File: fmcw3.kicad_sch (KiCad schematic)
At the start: 12 parts, among them P5 CONN_01X01, P7 CONN_01X01, P8 CONN_01X01, U4 ECS-TXO-3225MV, U6 NB3N551

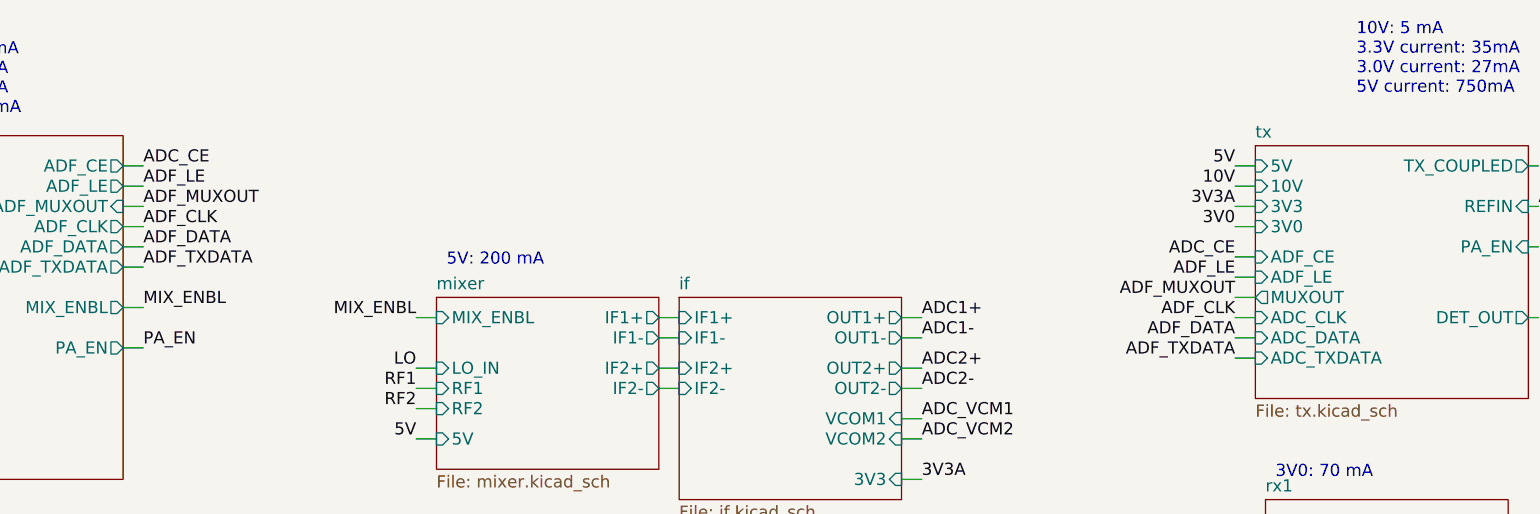
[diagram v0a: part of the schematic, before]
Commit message: 3 leds are added design is checked. Schematic pin name corrected
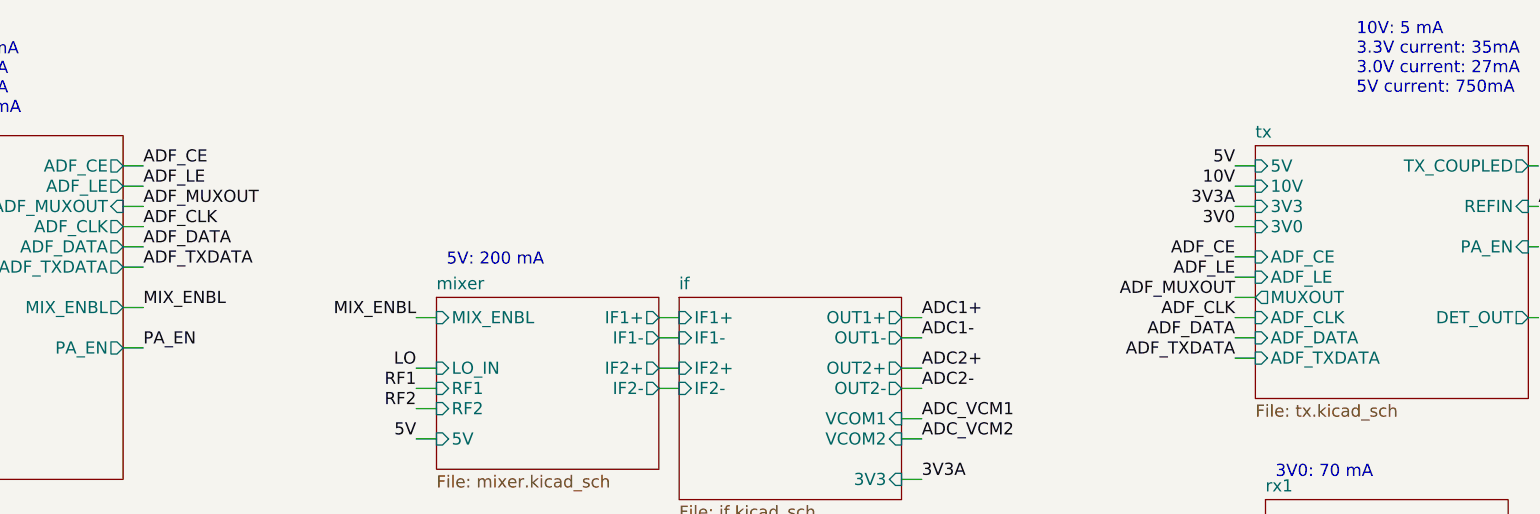
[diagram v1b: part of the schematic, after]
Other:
- sheet tx ports: added ADF_CLK, ADF_DATA, ADF_TXDATA; removed ADC_CLK, ADC_DATA, ADC_TXDATA
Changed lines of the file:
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@@
 		)
 	)
-	(label "ADC_CE"
+	(label "ADF_CE"
 		(at 83.82 46.99 0)
 		(effects
@@
 		)
 	)
-	(label "ADC_CE"
+	(label "ADF_CE"
 		(at 220.98 58.42 180)
 		(effects
@@
 			)
 		)
-		(pin "ADC_TXDATA" input
+		(pin "ADF_TXDATA" input
 			(at 223.52 71.12 180)
 			(effects
@@
 			)
 		)
-		(pin "ADC_CLK" input
+		(pin "ADF_CLK" input
 			(at 223.52 66.04 180)
 			(effects
@@
 			)
 		)
-		(pin "ADC_DATA" input
+		(pin "ADF_DATA" input
 			(at 223.52 68.58 180)
 			(effects

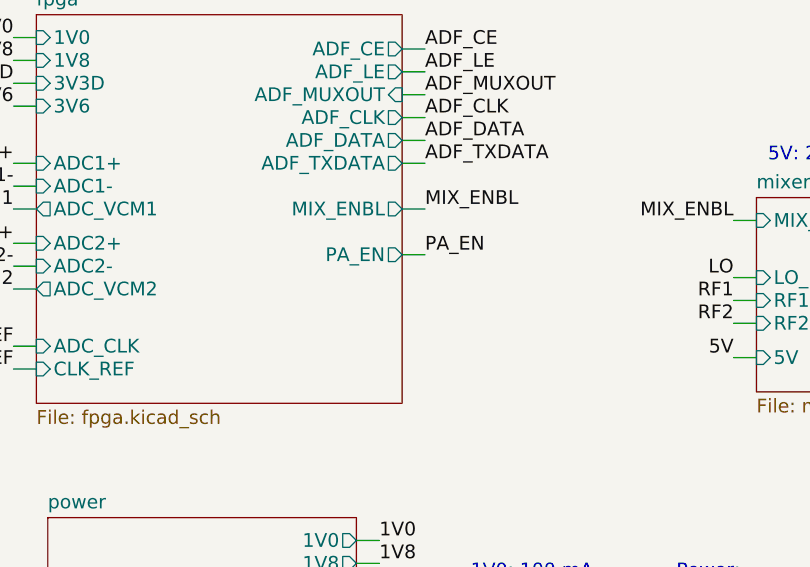
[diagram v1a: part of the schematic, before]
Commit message: Reset button is added. Detout is connected to an adc pin of fpga. Unused pad is deleted. Pins are check. Notes are added on pcb side. No problem related error drc excluded
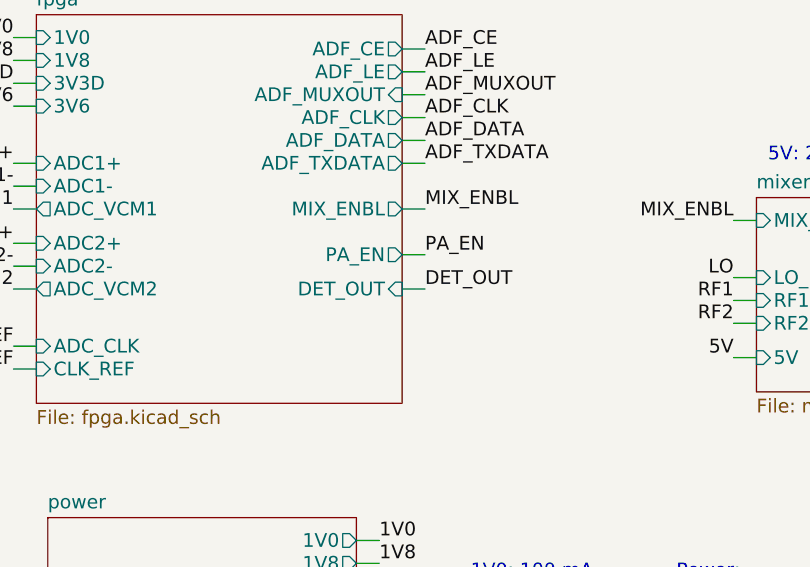
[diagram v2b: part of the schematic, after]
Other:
- sheet fpga ports: added DET_OUT; removed none
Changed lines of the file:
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@@
+	(wire
+		(pts
+			(xy 81.28 73.66) (xy 83.82 73.66)
+		)
+		(stroke
+			(width 0)
+			(type default)
+		)
+	)
 	(wire
 		(pts
@@
 			)
 			(justify right bottom)
+		)
+	)
+	(label "DET_OUT"
+		(at 83.82 73.66 0)
+		(effects
+			(font
+				(size 1.524 1.524)
+			)
+			(justify left bottom)
 		)
 	)
@@
 			(effects
 				(font
+					(size 1.524 1.524)
+				)
+				(justify right)
+			)
+		)
+		(pin "DET_OUT" input
+			(at 81.28 73.66 0)
+			(effects
+				(font

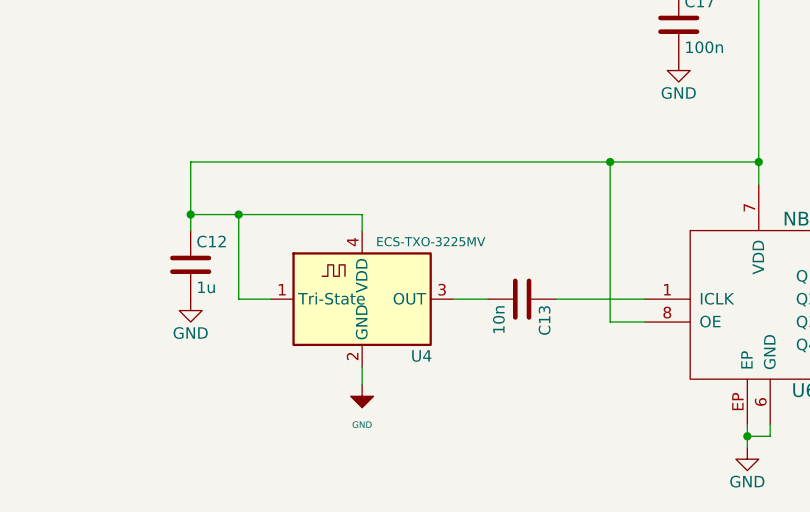
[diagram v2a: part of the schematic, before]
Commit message: Clock buffer path cap changed to resistor.
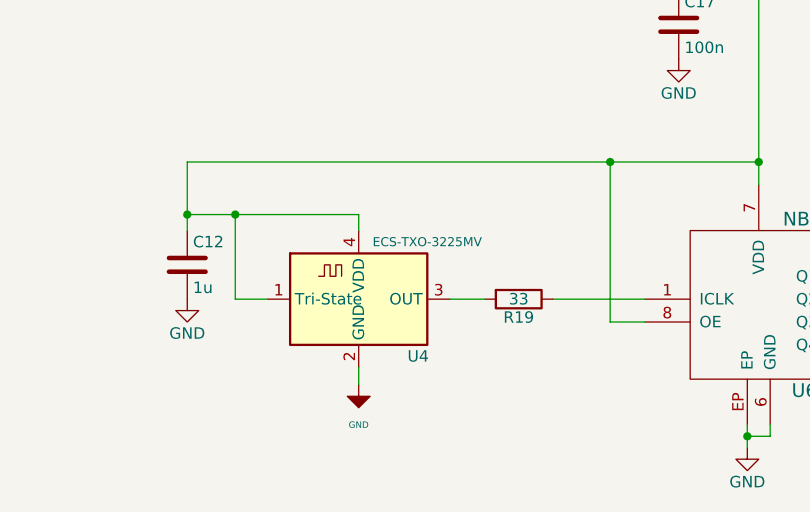
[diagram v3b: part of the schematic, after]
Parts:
- removed C13: 10n, Footprints:SMD_0402, symbol fmcw3-rescue:C
- added R19: 33, Footprints:SMD_0402, symbol fmcw3-rescue:R
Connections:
- net at U6.1 (ICLK): now also R19.1
- net at U4.3 (OUT): now also R19.2

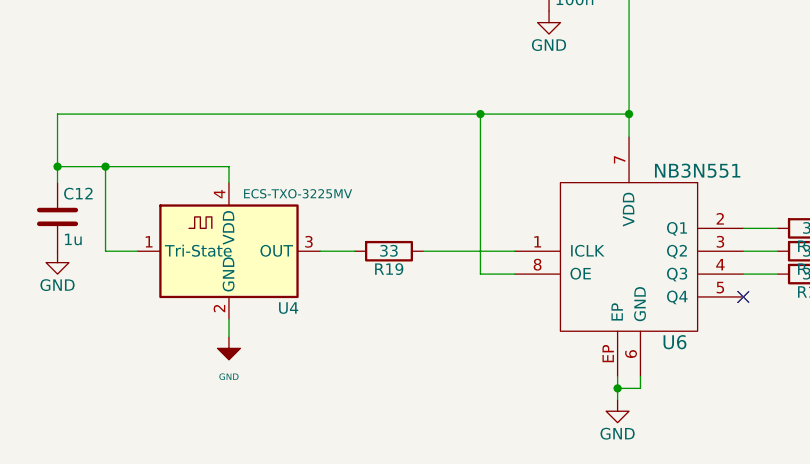
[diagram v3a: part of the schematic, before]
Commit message: Resistor value is changed to 0 ohm
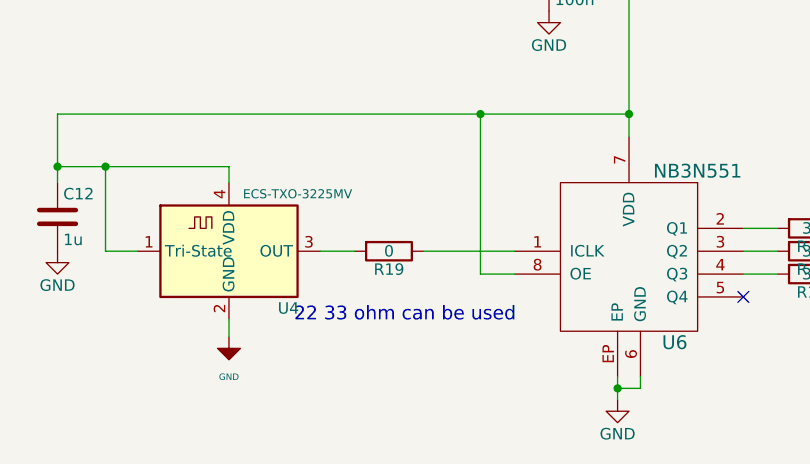
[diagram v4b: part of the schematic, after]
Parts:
- R19: value 33 -> 0
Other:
- note added: "22 33 ohm can be used"
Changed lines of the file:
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@@
+		)
+	)
+	(text "22 33 ohm can be used"
+		(exclude_from_sim no)
+		(at 105.918 178.562 0)
+		(effects
+			(font
+				(size 1.524 1.524)
+			)
 		)
 	)
@@
 			)
 		)
-		(property "Value" "33"
+		(property "Value" "0"
 			(at 104.14 171.45 90)
 			(effects

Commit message: final corrections is done. Working!
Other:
- sheet fpga ports: added 3V8; removed 3V6
- sheet power ports: added 3V8; removed 3V6
- note added: "1V0: 100 mA 1V8: 30 mA 3V0: 170 mA 5V: 900 mA 3.3VA: 540 mA 3.3VD: 100 mA 3V8: 80 mA 10V: 5 mA"
- note removed: "1V0: 100 mA 1V8: 30 mA 3V0: 170 mA 5V: 900 mA 3.3VA: 540 mA 3.3VD: 100 mA 3V6: 80 mA 10V: 5 mA"
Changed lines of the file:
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@@
 		)
 	)
-	(text "1V0: 100 mA\n1V8: 30 mA\n3V0: 170 mA\n5V: 900 mA\n3.3VA: 540 mA\n3.3VD: 100 mA\n3V6: 80 mA\n10V: 5 mA"
+	(text "1V0: 100 mA\n1V8: 30 mA\n3V0: 170 mA\n5V: 900 mA\n3.3VA: 540 mA\n3.3VD: 100 mA\n3V8: 80 mA\n10V: 5 mA"
 		(exclude_from_sim no)
 		(at 88.9 123.19 0)
@@
 		)
 	)
-	(label "3V6"
+	(label "3V8"
 		(at 78.74 121.92 0)
 		(effects
@@
 		)
 	)
-	(label "3V6"
+	(label "3V8"
 		(at 38.1 53.34 180)
 		(effects
@@
 			)
 		)
-		(pin "3V6" input
+		(pin "3V8" input
 			(at 40.64 53.34 180)
 			(effects
@@
 			)
 		)
-		(pin "3V6" output
+		(pin "3V8" output
 			(at 76.2 121.92 0)
 			(effects

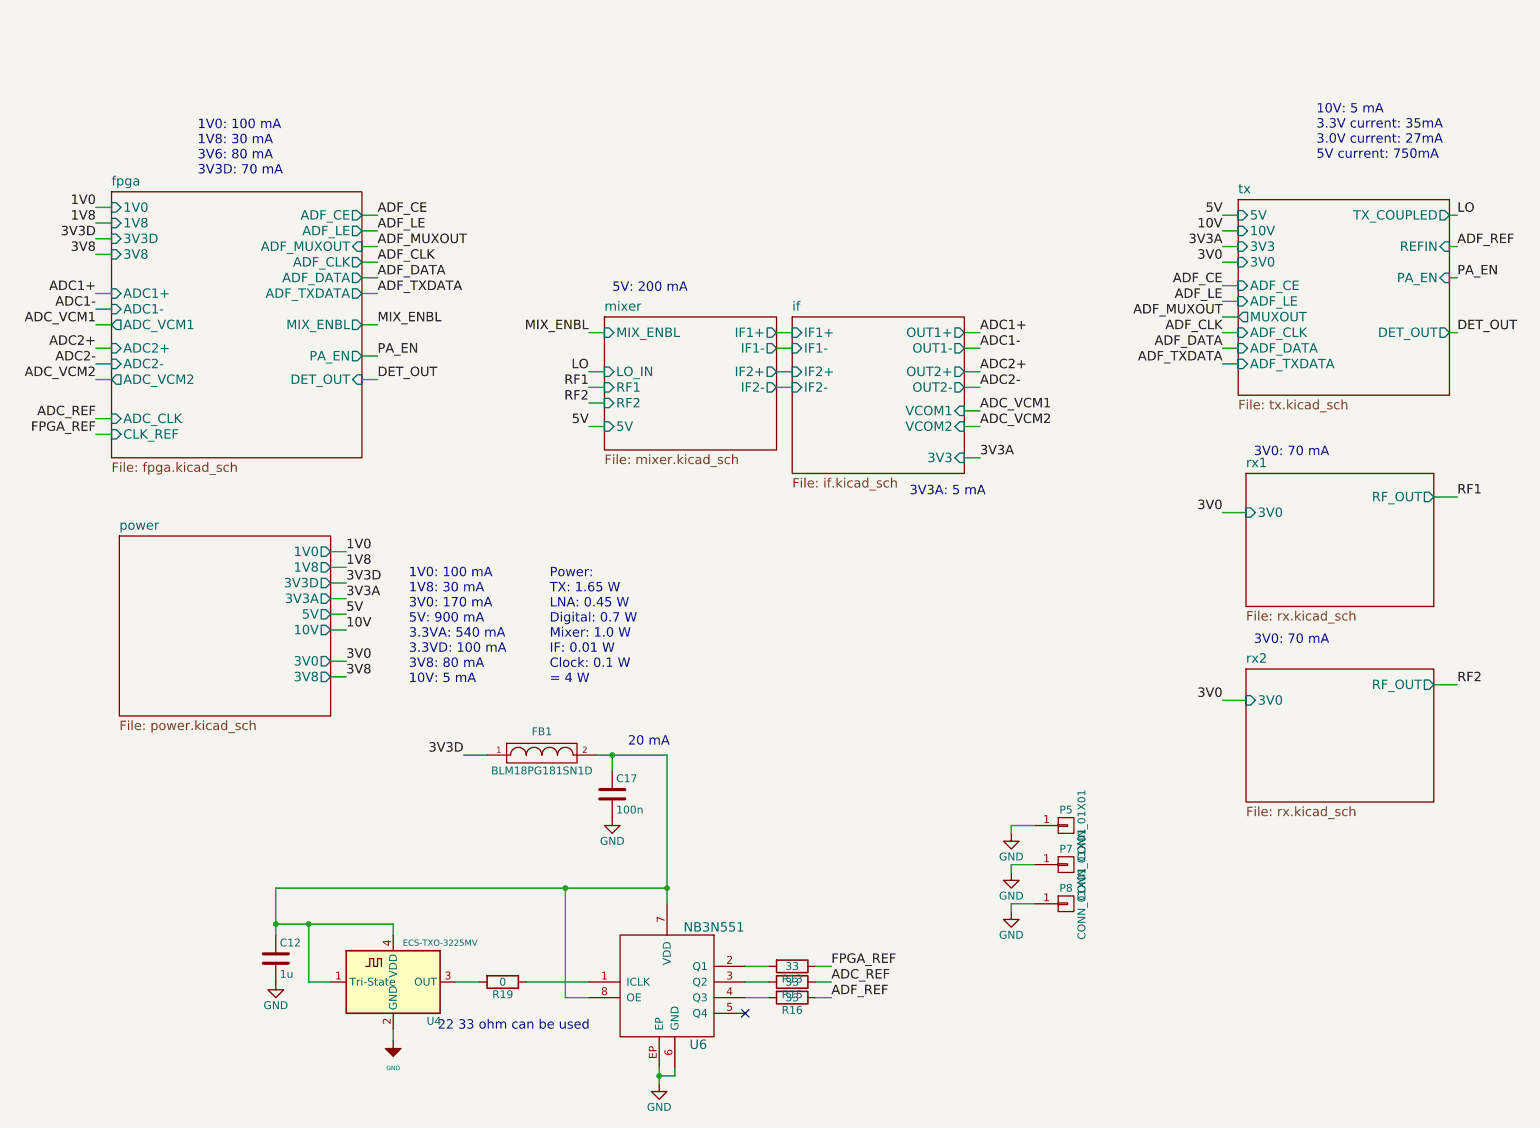
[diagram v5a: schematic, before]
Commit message: clock buffer and txco source is changed. Clock is clipped sin and fanout says cmos square out but it is better anyways. Also traces are 50 ohm as well. Copper pours other minor thinks are changed as well
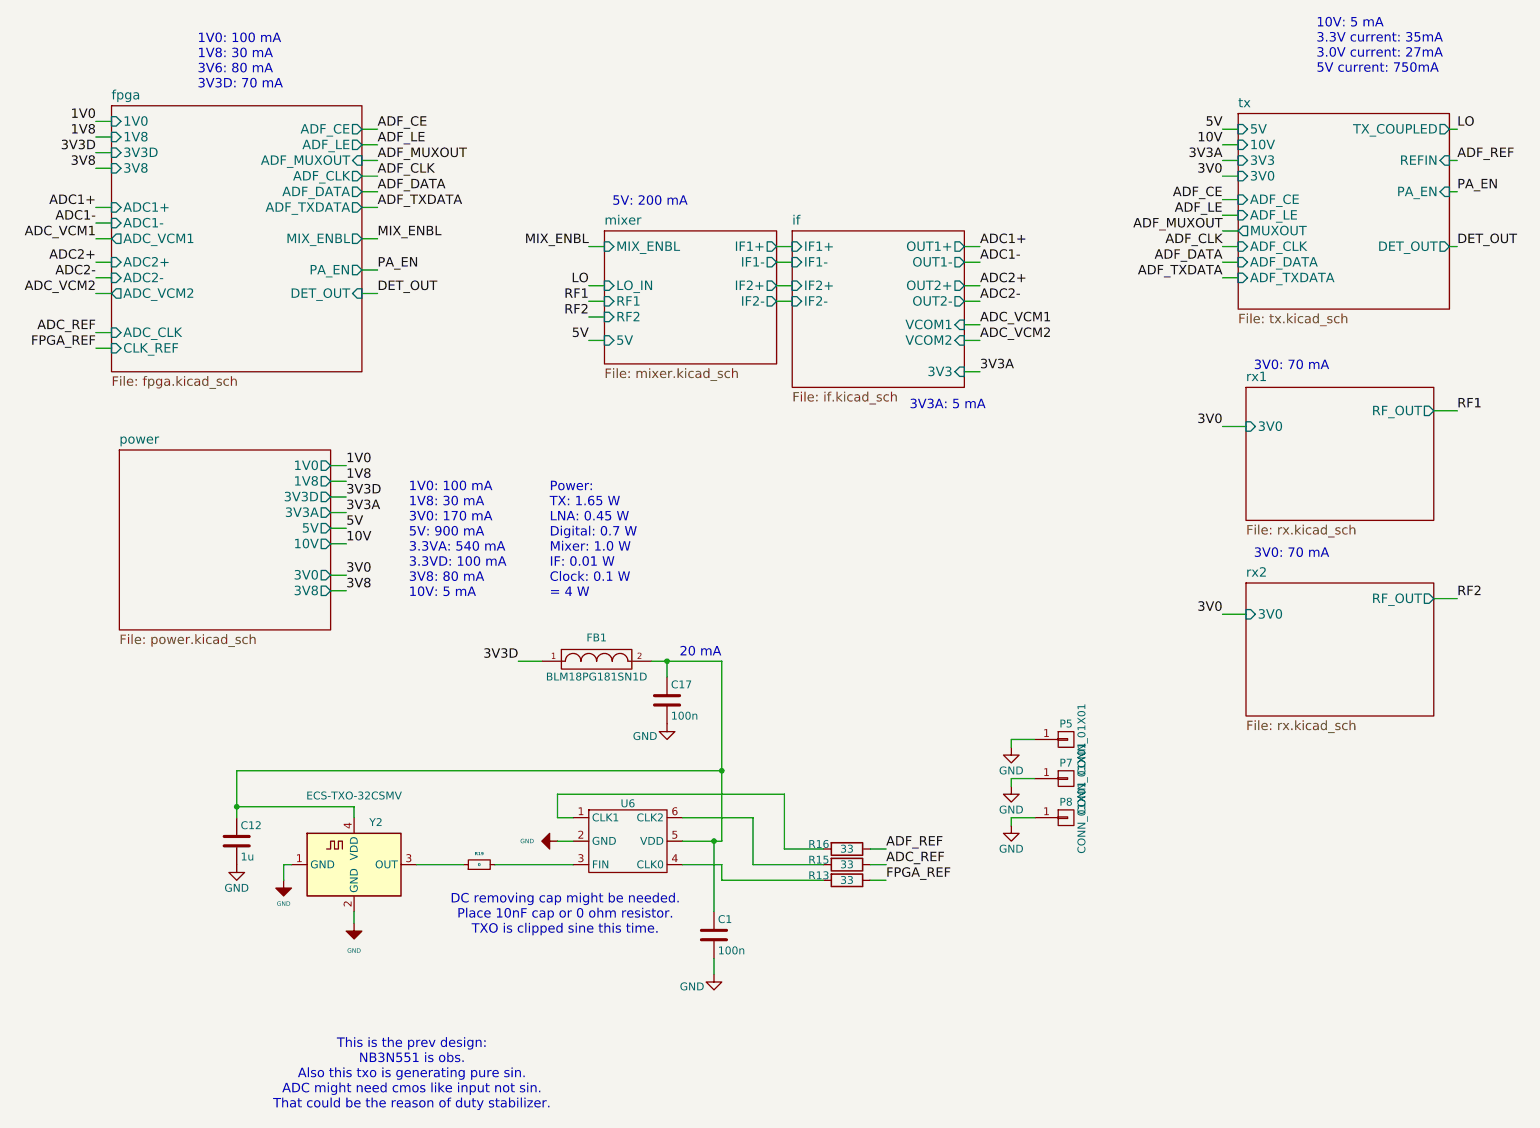
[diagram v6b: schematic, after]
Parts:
- removed R19: 0, Footprints:SMD_0402, symbol fmcw3-rescue:R
- removed U4: ECS-TXO-3225MV, Oscillator:Oscillator_SMD_EuroQuartz_XO32-4Pin_3.2x2.5mm, symbol Oscillator:ECS-2520MV-xxx-xx
- removed U6: NB3N551, fmcw3:DFN-8, symbol fmcw3:NB3N551
- added C1: 100n, Footprints:SMD_0402, symbol fmcw3-rescue:C
- added R19: 0, Footprints:SMD_0402, symbol Resistor:Resistor
- added U6: PL133-37, Footprints:SOT23_6, symbol PL133_37:PL133_37
- added Y2: ECS-TXO-32CSMV, Oscillator:Oscillator_SMD_ECS_2520MV-xxx-xx-4Pin_2.5x2.0mm, symbol ECS-TXO-32CSMV:ECS-TXO-32CSMV
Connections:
- net GND: now also C1.2, U6.2 (GND), Y2.1 (GND), Y2.2 (GND)
- net at C12.1, C17.1, FB1.2: now also C1.1, U6.5 (VDD), Y2.4 (VDD)
- net at R13.2: now also U6.4 (CLK0)
- net at R15.2: now also U6.6 (CLK2)
- net at R16.2: now also U6.1 (CLK1)
- new net: R19.1, Y2.3 (OUT)
- new net: R19.2, U6.3 (FIN)
- no-connect marks 1 -> 0
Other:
- note added: "DC removing cap might be needed. Place 10nF cap or 0 ohm resistor. TXO is clipped sine this time."
- note added: "This is the prev design: NB3N551 is obs. Also this txo is generating pure sin. ADC might need cmos like input not sin. That could be the reason of duty stabilizer."
- note removed: "22 33 ohm can be used"
- moved on the sheet: C12, C17, FB1, P5, P7, P8, R13, R15, R16
